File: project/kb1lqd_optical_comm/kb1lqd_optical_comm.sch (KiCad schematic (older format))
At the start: 9 parts

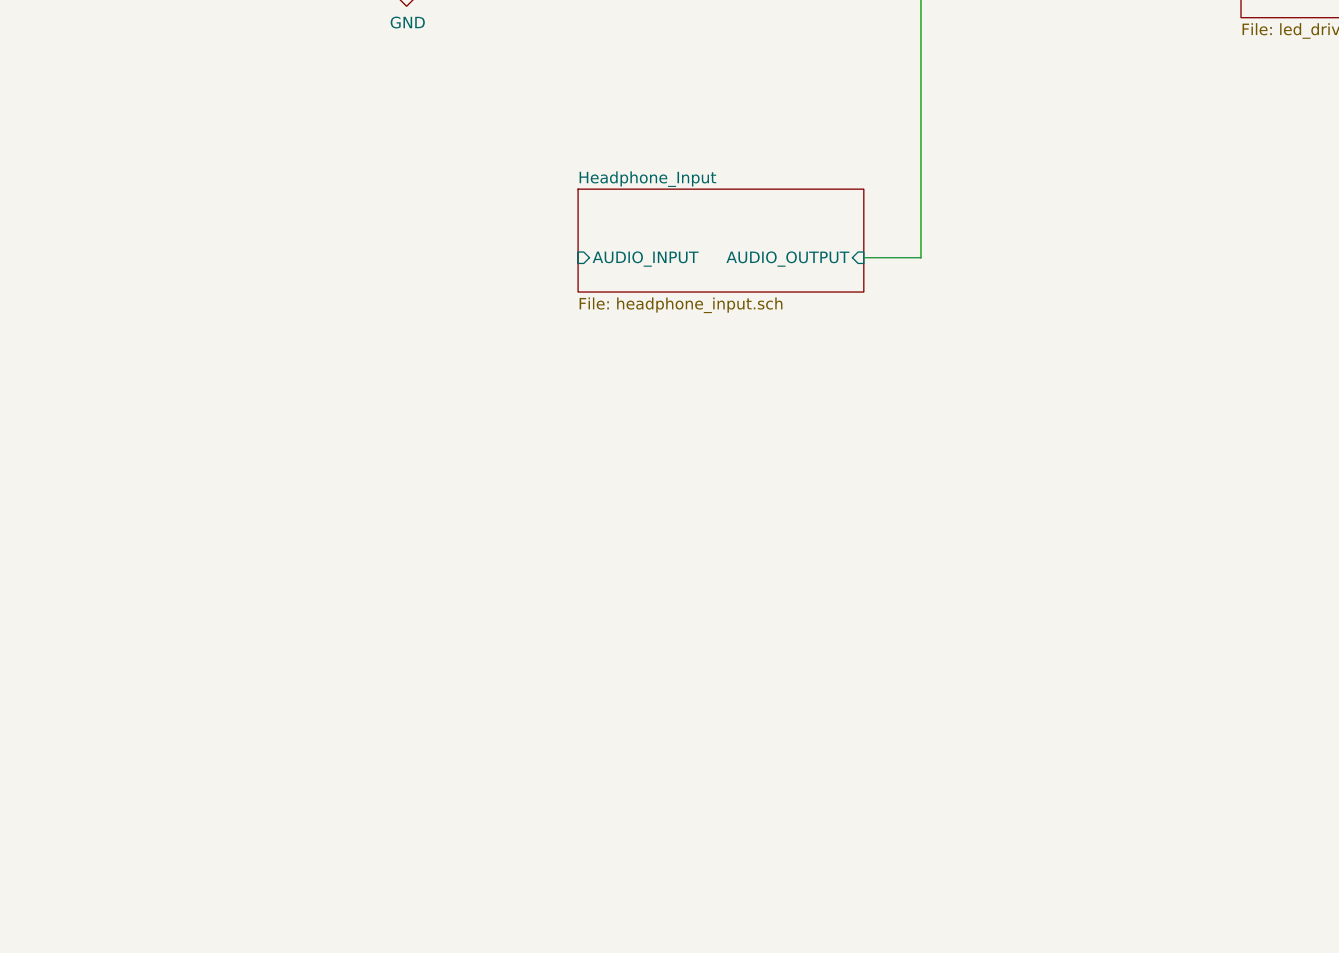
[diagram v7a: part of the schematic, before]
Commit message: adding recevier transimpedance amp. Adding simulations.
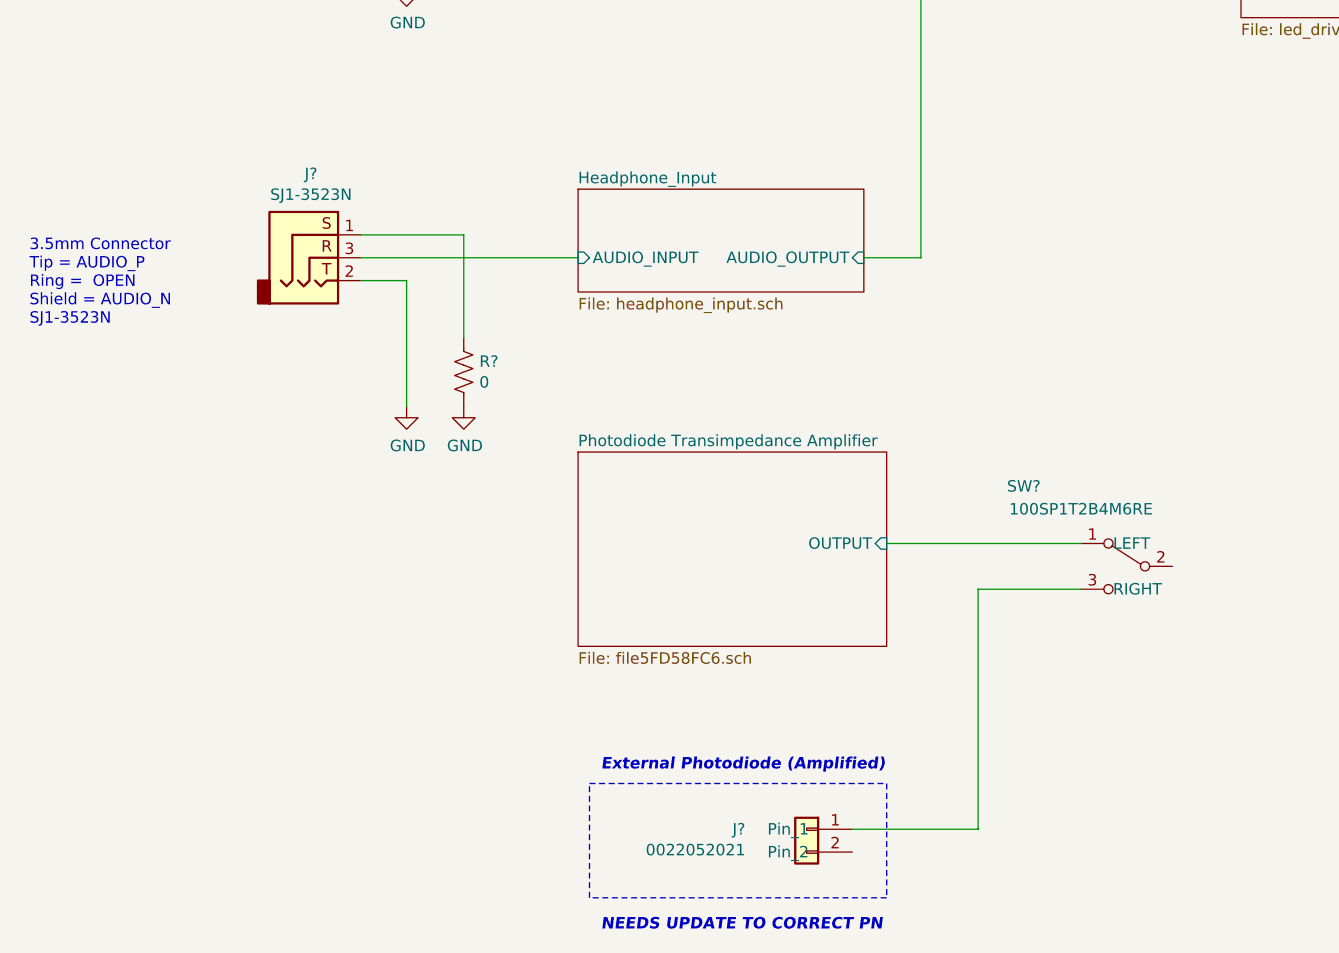
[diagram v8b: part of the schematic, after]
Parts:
- added J?: 0022052021, symbol kb1lqd_optical_comm:0022052021
- added J?: SJ1-3523N, symbol kb1lqd_optical_comm:SJ1-3523N
- added R?: 0, symbol Device:R_US
- added SW?: 100SP1T2B4M6RE, symbol kb1lqd_optical_comm:100SP1T2B4M6RE
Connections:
- net GND: now also J?.2, R?.2
- net Headphone_Input/AUDIO_INPUT: now also J?.3
- new net: J?.1 (Pin_1), SW?.3 (RIGHT)
- new net: J?.1, R?.1
- new net Photodiode Transimpedance Amplifier/OUTPUT: SW?.1 (LEFT)
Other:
- note added: "3.5mm Connector\nTip = AUDIO_P\nRing = OPEN\nShield = AUDIO_N\nSJ1-3523N"
- note added: "External Photodiode (Amplified)"
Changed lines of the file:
@@
 $Descr A 11000 8500
 encoding utf-8
-Sheet 1 4
+Sheet 1 5
 Title "KB1LQD Optical Communications 1"
 Date "2020-09-17"
@@
 	-1   0    0    -1
 $EndComp
+$Sheet
+S 3000 4950 1350 850
+U 5FD58FC7
+F0 "Photodiode Transimpedance Amplifier" 50
+F1 "file5FD58FC6.sch" 50
+F2 "OUTPUT" I R 4350 5350 50
+$EndSheet
+$Comp
+L kb1lqd_optical_comm:100SP1T2B4M6RE SW?
+U 1 1 5FD7D7DF
+P 5850 5600
+F 0 "SW?" H 6750 6100 50  0000 C CNN
+F 1 "100SP1T2B4M6RE" H 6500 6000 50  0000 C CNN
+F 2 "" H 5850 5600 50  0001 C CNN
+F 3 "" H 5850 5600 50  0001 C CNN
+	1    5850 5600
+	-1   0    0    -1
+$EndComp
+$Comp
+L kb1lqd_optical_comm:0022052021 J?
+U 1 1 5FD833A5
+P 4450 6750
+F 0 "J?" H 5168 6900 50  0000 L CNN
+F 1 "0022052021" H 5168 6809 50  0000 L CNN
+F 2 "" H 4450 6750 50  0001 C CNN
+F 3 "" H 4450 6750 50  0001 C CNN
+	1    4450 6750
+	-1   0    0    -1
+$EndComp
+Wire Wire Line
+	4350 5350 5200 5350
+Wire Wire Line
+	5200 5550 4750 5550
+Wire Wire Line
+	4750 5550 4750 6600
+Wire Wire Line
+	4750 6600 4200 6600
+Text Notes 3100 7050 0    50   Italic 10
+NEEDS UPDATE TO CORRECT PN
+Wire Notes Line
+	3050 6400 4350 6400
+Wire Notes Line
+	4350 6400 4350 6900
+Wire Notes Line
+	4350 6900 3050 6900
+Wire Notes Line
+	3050 6900 3050 6400
+Text Notes 3100 6350 0    50   Italic 10
+External Photodiode (Amplified)
+$Comp
+L kb1lqd_optical_comm:SJ1-3523N J?
+U 1 1 5FD93BCB
+P 1550 4350
+F 0 "J?" H 1832 4967 50  0000 C CNN
+F 1 "SJ1-3523N" H 1832 4876 50  0000 C CNN
+F 2 "" H 1550 4350 50  0001 C CNN
+F 3 "" H 1550 4350 50  0001 C CNN
+	1    1550 4350
+	1    0    0    -1
+$EndComp
+Text Notes 600  4400 0    50   ~ 0
+3.5mm Connector\nTip = AUDIO_P\nRing =  OPEN\nShield = AUDIO_N\nSJ1-3523N
+$Comp
+L Device:R_US R?
+U 1 1 5FD94DA4
+P 2500 4600
+F 0 "R?" H 2568 4646 50  0000 L CNN
+F 1 "0" H 2568 4555 50  0000 L CNN
+F 2 "" V 2540 4590 50  0001 C CNN
+F 3 "~" H 2500 4600 50  0001 C CNN
+	1    2500 4600
+	1    0    0    -1
+$EndComp
+Wire Wire Line
+	2050 4100 3000 4100
+Wire Wire Line
+	2050 4000 2500 4000
+Wire Wire Line
+	2500 4000 2500 4450
+Wire Wire Line
+	2050 4200 2250 4200
+Wire Wire Line
+	2250 4200 2250 4750
+$Comp
+L power:GND #PWR?
+U 1 1 5FD984FE
+P 2250 4750
+F 0 "#PWR?" H 2250 4500 50  0001 C CNN
+F 1 "GND" H 2255 4577 50  0000 C CNN
+F 2 "" H 2250 4750 50  0001 C CNN
+F 3 "" H 2250 4750 50  0001 C CNN
+	1    2250 4750
+	1    0    0    -1
+$EndComp
+$Comp
+L power:GND #PWR?
+U 1 1 5FD987E2
+P 2500 4750
+F 0 "#PWR?" H 2500 4500 50  0001 C CNN
+F 1 "GND" H 2505 4577 50  0000 C CNN
+F 2 "" H 2500 4750 50  0001 C CNN
+F 3 "" H 2500 4750 50  0001 C CNN
+	1    2500 4750
+	1    0    0    -1
+$EndComp
 $EndSCHEMATC
